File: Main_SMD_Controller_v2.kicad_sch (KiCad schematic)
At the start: 76 parts, among them J101 ETB43034G000Z, J102 ETB43034G000Z, J103 B2B-XH-A, J104 PH-1X3SG, J105 PCB-20, J106 B2B-XH-A, J107 PCB-20, J108 PH-1X2SG, J109 PCB-20, J110 PCB-20, P101 Eoshi-chan_Silk, P102 Serial_QR, U101 XC6201P332MR-G, U102 XC6902N331MR-G, U103 TC4066BP, U104 ADA4510-2ARZ, U105 MCP1501-20E/CHY, U106 LT1167CN8, U107 NJU7098A

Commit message: 念のため
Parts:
- J103: value B2B-XH-A -> B2P3-VH-3.3(LF)(SN); footprint Connector_JST:JST_XH_B2B-XH-A_1x02_P2.50mm_Vertical -> Connector_JST:JST_VH_B2P3-VH_1x02_P7.92mm_Vertical
- R107, R110, R111: footprint Resistor_THT:R_Axial_DIN0207_L6.3mm_D2.5mm_P2.54mm_Vertical -> Resistor_THT:R_Axial_DIN0207_L6.3mm_D2.5mm_P10.16mm_Horizontal
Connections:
- net GAIN2: now also U103.12; no longer U103.6
- net GAIN3: now also U103.6; no longer U103.12
- net ADC_Vref: now reaches R112.1, TP103.1, U105.1 (OUT)
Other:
- sheet Interface ports: added ADC_Vref; removed none
- note added: "Memo: GAIN2,3を入れ替える GreenPAKのFWを変更"
- moved on the sheet: TP103
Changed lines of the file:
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@@
 		)
 	)
+	(text "Memo: GAIN2,3を入れ替える GreenPAKのFWを変更"
+		(exclude_from_sim no)
+		(at 142.24 116.84 0)
+		(effects
+			(font
+				(size 1.27 1.27)
+			)
+		)
+	)
 	(text "V_{IN}=1/40*V_{SENS}"
 		(exclude_from_sim no)
@@
 	(text "2.048V"
 		(exclude_from_sim no)
-		(at 208.28 130.81 0)
+		(at 208.28 134.62 0)
 		(effects
 			(font
@@
 	)
 	(junction
-		(at 213.36 132.08)
-		(diameter 0)
-		(color 0 0 0 0)
-	)
-	(junction
 		(at 67.31 162.56)
 		(diameter 0)
@@
 	)
 	(junction
+		(at 204.47 132.08)
+		(diameter 0)
+		(color 0 0 0 0)
+	)
+	(junction
 		(at 181.61 124.46)
 		(diameter 0)
@@
 	(wire
 		(pts
-			(xy 213.36 128.27) (xy 213.36 132.08)
+			(xy 204.47 128.27) (xy 204.47 132.08)
 		)
 		(stroke
@@
 	(wire
 		(pts
+			(xy 204.47 132.08) (xy 213.36 132.08)
+		)
+		(stroke
+			(width 0)
+			(type default)
+		)
+	)
+	(wire
+		(pts
 			(xy 116.84 26.67) (xy 121.92 26.67)
 		)
@@
 	(wire
 		(pts
-			(xy 203.2 132.08) (xy 213.36 132.08)
+			(xy 203.2 132.08) (xy 204.47 132.08)
+		)
+		(stroke
+			(width 0)
+			(type default)
+		)
+	)
+	(wire
+		(pts
+			(xy 57.15 63.5) (xy 59.69 63.5)
 		)
 		(stroke
@@
 		)
 	)
+	(label "GAIN2"
+		(at 121.92 113.03 0)
+		(effects
+			(font
+				(size 1.27 1.27)
+			)
+			(justify left bottom)
+		)
+	)
 	(label "Vmeas"
 		(at 59.69 58.42 0)
@@
 		)
 	)
+	(label "ADC_Vref"
+		(at 213.36 132.08 0)
+		(effects
+			(font
+				(size 1.27 1.27)
+			)
+			(justify left bottom)
+		)
+	)
+	(label "ADC_Vref"
+		(at 59.69 63.5 0)
+		(effects
+			(font
+				(size 1.27 1.27)
+			)
+			(justify left bottom)
+		)
+	)
 	(label "rt"
 		(at 220.98 63.5 180)
@@
 		)
 	)
+	(label "GAIN3"
+		(at 121.92 101.6 0)
+		(effects
+			(font
+				(size 1.27 1.27)
+			)
+			(justify left bottom)
+		)
+	)
 	(label "RLY_LOUT"
 		(at 59.69 48.26 0)
@@
 		)
 	)
-	(label "GAIN2"
-		(at 121.92 101.6 0)
-		(effects
-			(font
-				(size 1.27 1.27)
-			)
-			(justify left bottom)
-		)
-	)
 	(label "Imeas"
 		(at 201.93 87.63 180)
@@
 		)
 	)
-	(label "GAIN3"
-		(at 121.92 113.03 0)
-		(effects
-			(font
-				(size 1.27 1.27)
-			)
-			(justify left bottom)
-		)
-	)
 	(label "RLY_LOUT"
 		(at 238.76 33.02 180)
@@
 			)
 		)
-		(property "Value" "B2B-XH-A"
+		(property "Value" "B2P3-VH-3.3(LF)(SN)"
 			(at 212.09 29.2099 0)
 			(show_name no)
@@
 			)
 		)
-		(property "Footprint" "Connector_JST:JST_XH_B2B-XH-A_1x02_P2.50mm_Vertical"
+		(property "Footprint" "Connector_JST:JST_VH_B2P3-VH_1x02_P7.92mm_Vertical"
 			(at 209.55 26.67 0)
 			(hide yes)
@@
 	(symbol
 		(lib_id "Connector:TestPoint_Probe")
-		(at 213.36 128.27 0)
+		(at 204.47 128.27 0)
 		(unit 1)
 		(body_style 1)
@@
 		(dnp no)
 		(property "Reference" "TP103"
-			(at 217.17 125.73 0)
+			(at 208.28 125.73 0)
 			(show_name no)
 			(do_not_autoplace no)
@@
 		)
 		(property "Value" "RCTCTE"
-			(at 217.17 128.27 0)
+			(at 208.28 128.27 0)
 			(show_name no)
 			(do_not_autoplace no)
@@
 		)
 		(property "Footprint" "AM_Conn_TP:RCTCE"
-			(at 218.44 128.27 0)
+			(at 209.55 128.27 0)
 			(hide yes)
 			(show_name no)
@@
 		)
 		(property "Datasheet" ""
-			(at 218.44 128.27 0)
+			(at 209.55 128.27 0)
 			(hide yes)
 			(show_name no)
@@
 		)
 		(property "Description" "test point (alternative probe-style design)"
-			(at 213.36 128.27 0)
+			(at 204.47 128.27 0)
 			(hide yes)
 			(show_name no)
@@
 		)
 		(property "Description_1" ""
-			(at 213.36 128.27 0)
+			(at 204.47 128.27 0)
 			(hide yes)
 			(show_name no)
@@
 		)
 		(property "Sengoku_code" ""
-			(at 213.36 128.27 0)
+			(at 204.47 128.27 0)
 			(hide yes)
 			(show_name no)
@@
 			)
 		)
-		(property "Footprint" "Resistor_THT:R_Axial_DIN0207_L6.3mm_D2.5mm_P2.54mm_Vertical"
+		(property "Footprint" "Resistor_THT:R_Axial_DIN0207_L6.3mm_D2.5mm_P10.16mm_Horizontal"
 			(at 163.83 28.448 90)
 			(hide yes)
@@
 			)
 		)
-		(property "Footprint" "Resistor_THT:R_Axial_DIN0207_L6.3mm_D2.5mm_P2.54mm_Vertical"
+		(property "Footprint" "Resistor_THT:R_Axial_DIN0207_L6.3mm_D2.5mm_P10.16mm_Horizontal"
 			(at 204.978 48.26 90)
 			(hide yes)
@@
 			)
 		)
-		(property "Footprint" "Resistor_THT:R_Axial_DIN0207_L6.3mm_D2.5mm_P2.54mm_Vertical"
+		(property "Footprint" "Resistor_THT:R_Axial_DIN0207_L6.3mm_D2.5mm_P10.16mm_Horizontal"
 			(at 204.978 58.42 90)
 			(hide yes)
@@
 		(members "403ef226-6633-4c83-ab8a-01415e3ffac7" "ab16d228-7bd2-4212-bd9b-7f549ffd1b8f")
 	)
-	(group ""
-		(members "403ef226-6633-4c83-ab8a-01415e3ffac7" "ab16d228-7bd2-4212-bd9b-7f549ffd1b8f")
-	)
 	(sheet
 		(at 223.52 58.42)
@@
 	(sheet
 		(at 40.64 34.29)
-		(size 16.51 30.48)
+		(size 16.51 31.75)
 		(exclude_from_sim no)
 		(in_bom yes)
@@
 		)
 		(property "Sheetfile" "v2_interface.kicad_sch"
-			(at 40.64 65.786 0)
+			(at 40.64 67.31 0)
 			(show_name no)
 			(do_not_autoplace no)
@@
 			(effects
 				(font
+					(size 1.27 1.27)
+				)
+				(justify right)
+			)
+		)
+		(pin "ADC_Vref" input
+			(at 57.15 63.5 0)
+			(effects
+				(font

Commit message: 部品配置
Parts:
- added R117: 0, Resistor_SMD:R_0805_2012Metric, symbol Device:R
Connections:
- net GND: now also R117.2
- net GNDA: now also R117.1
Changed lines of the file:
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@@
 	)
 	(junction
+		(at 191.77 62.23)
+		(diameter 0)
+		(color 0 0 0 0)
+	)
+	(junction
 		(at 147.32 39.37)
 		(diameter 0)
@@
 	(wire
 		(pts
+			(xy 181.61 62.23) (xy 180.34 62.23)
+		)
+		(stroke
+			(width 0)
+			(type default)
+		)
+	)
+	(wire
+		(pts
 			(xy 52.07 128.27) (xy 52.07 130.81)
 		)
@@
 	(wire
 		(pts
-			(xy 213.36 156.21) (xy 213.36 158.75)
+			(xy 189.23 62.23) (xy 191.77 62.23)
 		)
 		(stroke
@@
 	(wire
 		(pts
-			(xy 228.6 102.87) (xy 228.6 105.41)
+			(xy 213.36 156.21) (xy 213.36 158.75)
 		)
 		(stroke
@@
 	(wire
 		(pts
+			(xy 191.77 62.23) (xy 191.77 63.5)
+		)
+		(stroke
+			(width 0)
+			(type default)
+		)
+	)
+	(wire
+		(pts
 			(xy 158.75 73.66) (xy 160.02 73.66)
 		)
@@
 	(wire
 		(pts
+			(xy 237.49 102.87) (xy 238.76 102.87)
+		)
+		(stroke
+			(width 0)
+			(type default)
+		)
+	)
+	(wire
+		(pts
 			(xy 104.14 170.18) (xy 104.14 172.72)
 		)
@@
 	(wire
 		(pts
+			(xy 203.2 63.5) (xy 203.2 62.23)
+		)
+		(stroke
+			(width 0)
+			(type default)
+		)
+	)
+	(wire
+		(pts
 			(xy 57.15 41.91) (xy 67.31 41.91)
 		)
@@
 	(wire
 		(pts
-			(xy 229.87 102.87) (xy 228.6 102.87)
-		)
-		(stroke
-			(width 0)
-			(type default)
-		)
-	)
-	(wire
-		(pts
 			(xy 148.59 85.09) (xy 151.13 85.09)
 		)
@@
 	(wire
 		(pts
-			(xy 238.76 92.71) (xy 238.76 102.87)
+			(xy 180.34 62.23) (xy 180.34 63.5)
 		)
 		(stroke
@@
 	(wire
 		(pts
+			(xy 228.6 102.87) (xy 229.87 102.87)
+		)
+		(stroke
+			(width 0)
+			(type default)
+		)
+	)
+	(wire
+		(pts
 			(xy 212.09 85.09) (xy 213.36 85.09)
 		)
@@
 		)
 	)
+	(wire
+		(pts
+			(xy 228.6 102.87) (xy 228.6 105.41)
+		)
+		(stroke
+			(width 0)
+			(type default)
+		)
+	)
 	(bus
 		(pts
@@
 	(wire
 		(pts
-			(xy 237.49 102.87) (xy 238.76 102.87)
-		)
-		(stroke
-			(width 0)
-			(type default)
-		)
-	)
-	(wire
-		(pts
 			(xy 113.03 73.66) (xy 113.03 85.09)
 		)
@@
 		)
 	)
+	(wire
+		(pts
+			(xy 238.76 92.71) (xy 238.76 102.87)
+		)
+		(stroke
+			(width 0)
+			(type default)
+		)
+	)
 	(table
 		(column_count 2)
@@
 	)
 	(symbol
+		(lib_name "GND_1")
+		(lib_id "power:GND")
+		(at 180.34 63.5 0)
+		(unit 1)
+		(body_style 1)
+		(exclude_from_sim no)
+		(in_bom yes)
+		(on_board yes)
+		(in_pos_files yes)
+		(dnp no)
+		(fields_autoplaced yes)
+		(property "Reference" "#PWR0145"
+			(at 180.34 69.85 0)
+			(hide yes)
+			(show_name no)
+			(do_not_autoplace no)
+			(effects
+				(font
+					(size 1.27 1.27)
+				)
+			)
+		)
+		(property "Value" "GND"
+			(at 180.34 68.58 0)
+			(show_name no)
+			(do_not_autoplace no)
+			(effects
+				(font
+					(size 1.27 1.27)
+				)
+			)
+		)
+		(property "Footprint" ""
+			(at 180.34 63.5 0)
+			(hide yes)
+			(show_name no)
+			(do_not_autoplace no)
+			(effects
+				(font
+					(size 1.27 1.27)
+				)
+			)
+		)
+		(property "Datasheet" ""
+			(at 180.34 63.5 0)
+			(hide yes)
+			(show_name no)
+			(do_not_autoplace no)
+			(effects
+				(font
+					(size 1.27 1.27)
+				)
+			)
+		)
+		(property "Description" "Power symbol creates a global label with name \"GND\" , ground"
+			(at 180.34 63.5 0)
+			(hide yes)
+			(show_name no)
+			(do_not_autoplace no)
+			(effects
+				(font
+					(size 1.27 1.27)
+				)
+			)
+		)
+		(pin "1"
+		)
+		(instances
+			(project "Main_SMD_Controller_v2"
+				(path "/ad678d38-2bf7-47ec-94cd-212edb6f07b2"
+					(reference "#PWR0145")
+					(unit 1)
+				)
+			)
+		)
+	)
+	(symbol
 		(lib_id "power:-3V3")
 		(at 170.18 55.88 180)
@@
 	(symbol
 		(lib_id "power:GNDA")
-		(at 203.2 62.23 0)
+		(at 203.2 63.5 0)
 		(unit 1)
 		(body_style 1)
@@
 		(fields_autoplaced yes)
 		(property "Reference" "#PWR0126"
-			(at 203.2 68.58 0)
+			(at 203.2 69.85 0)
 			(hide yes)
 			(show_name no)
@@
 		)
 		(property "Value" "GNDA"
-			(at 203.2 67.31 0)
+			(at 203.2 68.58 0)
 			(show_name no)
 			(do_not_autoplace no)
@@
 		)
 		(property "Footprint" ""
-			(at 203.2 62.23 0)
+			(at 203.2 63.5 0)
 			(hide yes)
 			(show_name no)
@@
 		)
 		(property "Datasheet" ""
-			(at 203.2 62.23 0)
+			(at 203.2 63.5 0)
 			(hide yes)
 			(show_name no)
@@
 		)
 		(property "Description" "Power symbol creates a global label with name \"GNDA\" , analog ground"
-			(at 203.2 62.23 0)
+			(at 203.2 63.5 0)
 			(hide yes)
 			(show_name no)
@@
 	(symbol
 		(lib_id "power:GNDA")
-		(at 191.77 62.23 0)
+		(at 191.77 63.5 0)
 		(unit 1)
 		(body_style 1)
@@
 		(fields_autoplaced yes)
 		(property "Reference" "#PWR0122"
-			(at 191.77 68.58 0)
+			(at 191.77 69.85 0)
 			(hide yes)
 			(show_name no)
@@
 		)
 		(property "Value" "GNDA"
-			(at 191.77 67.31 0)
+			(at 191.77 68.58 0)
 			(show_name no)
 			(do_not_autoplace no)
@@
 		)
 		(property "Footprint" ""
-			(at 191.77 62.23 0)
+			(at 191.77 63.5 0)
 			(hide yes)
 			(show_name no)
@@
 		)
 		(property "Datasheet" ""
-			(at 191.77 62.23 0)
+			(at 191.77 63.5 0)
 			(hide yes)
 			(show_name no)
@@
 		)
 		(property "Description" "Power symbol creates a global label with name \"GNDA\" , analog ground"
-			(at 191.77 62.23 0)
+			(at 191.77 63.5 0)
 			(hide yes)
 			(show_name no)
@@
 					(unit 1)
 				)
+			)
+		)
+	)
+	(symbol
+		(lib_id "Device:R")
+		(at 185.42 62.23 270)
+		(unit 1)
+		(body_style 1)
+		(exclude_from_sim no)
+		(in_bom yes)
+		(on_board yes)
+		(in_pos_files yes)
+		(dnp no)
+		(property "Reference" "R117"
+			(at 185.42 66.04 90)
+			(show_name no)
+			(do_not_autoplace no)
+			(effects
+				(font
+					(size 1.27 1.27)
+				)
+			)
+		)
+		(property "Value" "0"
+			(at 185.42 68.58 90)
+			(show_name no)
+			(do_not_autoplace no)
+			(effects
+				(font
+					(size 1.27 1.27)
+				)
+			)
+		)
+		(property "Footprint" "Resistor_SMD:R_0805_2012Metric"
+			(at 185.42 60.452 90)
+			(hide yes)
+			(show_name no)
+			(do_not_autoplace no)
+			(effects
+				(font
+					(size 1.27 1.27)
+				)
+			)
+		)
+		(property "Datasheet" ""
+			(at 185.42 62.23 0)
+			(hide yes)
+			(show_name no)
+			(do_not_autoplace no)
+			(effects
+				(font
+					(size 1.27 1.27)
+				)
+			)
+		)
+		(property "Description" "Resistor"
+			(at 185.42 62.23 0)
+			(hide yes)
+			(show_name no)
+			(do_not_autoplace no)
+			(effects
+				(font
+					(size 1.27 1.27)
+				)
+			)
+		)
+		(pin "2"
+		)
+		(pin "1"
+		)
+		(instances
+			(project "Main_SMD_Controller_v2"
+				(path "/ad678d38-2bf7-47ec-94cd-212edb6f07b2"
+					(reference "R117")
+					(unit 1)
+				)

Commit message: ほぼ完成?
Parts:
- added C124, C125: 47u, Capacitor_SMD:CP_Elec_6.3x5.9, symbol Device:C_Polarized_Small
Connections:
- net GND: now also C124.2, C125.1
- net VCC: now also C124.1
- net VEE: now also C125.2

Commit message: ほぼ完成
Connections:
- net GNDA: now also U104.3; no longer U104.5
- net Vin: now also U104.5; no longer U104.3
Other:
- moved on the sheet: C118

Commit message: アノテーション変更前
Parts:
- added J111: B2B-XH-A, Connector_JST:JST_XH_B2B-XH-A_1x02_P2.50mm_Vertical, symbol Connector_Generic:Conn_01x02
- added J112: PH-1X3SG, Connector_PinHeader_2.54mm:PinHeader_1x03_P2.54mm_Vertical, symbol Connector_Generic:Conn_01x03
- FB101, FB102: footprint Inductor_SMD:L_0805_2012Metric -> Inductor_THT:L_Axial_L5.3mm_D2.2mm_P2.54mm_Vertical_Vishay_IM-1
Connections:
- net GND: now also J111.2 (Pin_2)
- net rt: now also J112.2 (Pin_2)
- new net: J111.1 (Pin_1), J112.3 (Pin_3)
- new net Interface/rt: J112.1 (Pin_1)

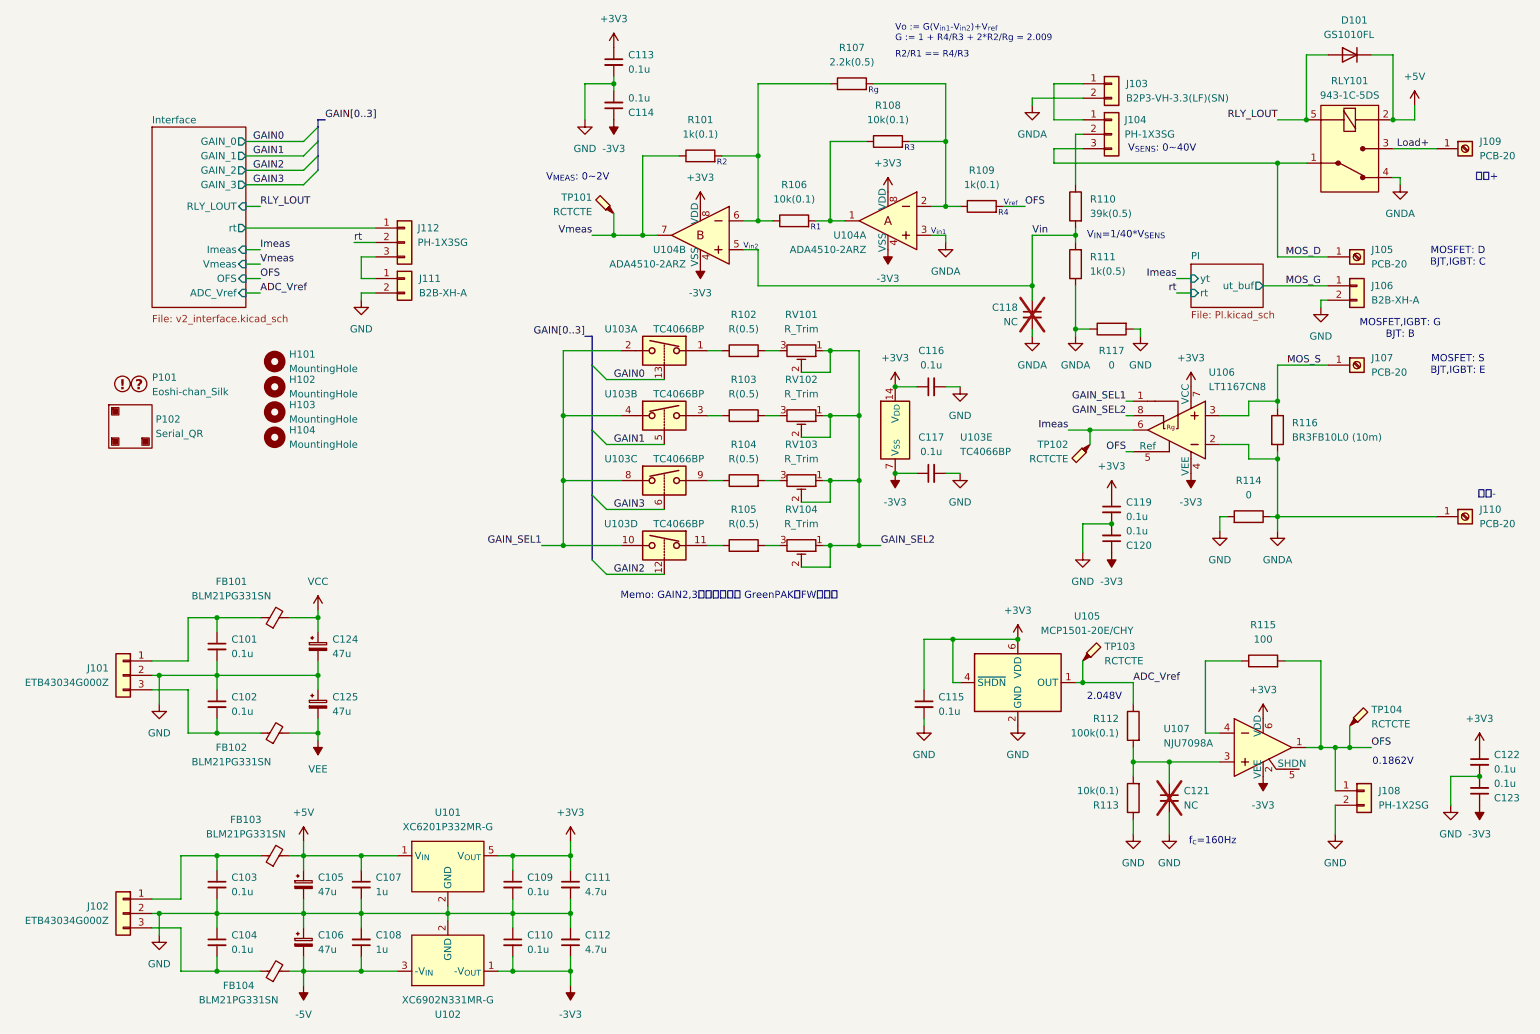
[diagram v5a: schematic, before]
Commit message: アノテーションリセット 余計なもんも消す
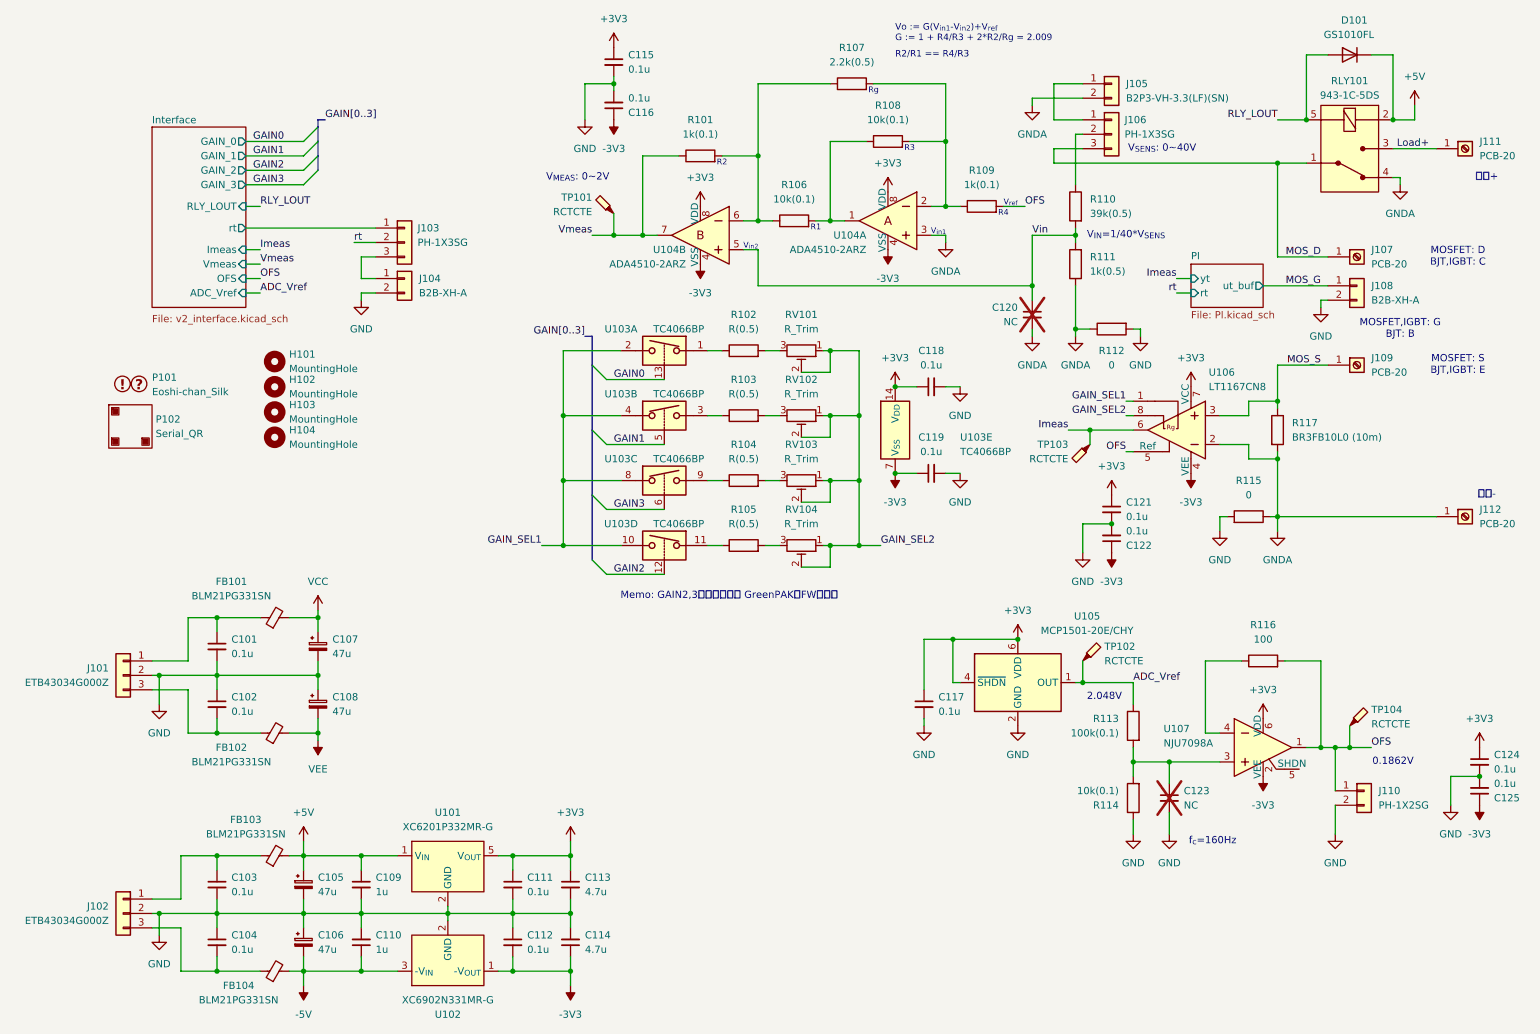
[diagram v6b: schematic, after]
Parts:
- renumbered C124 to C107, C125 to C108, C107 to C109, C108 to C110, C109 to C111, C110 to C112, C111 to C113, C112 to C114, C113 to C115, C114 to C116, C115 to C117, C116 to C118, C117 to C119, C118 to C120, C119 to C121, C120 to C122, C121 to C123, C122 to C124, C123 to C125, J112 to J103, J111 to J104, J103 to J105, J104 to J106, J105 to J107, J106 to J108, J107 to J109, J108 to J110, J109 to J111, J110 to J112, R117 to R112, R112 to R113, R113 to R114, R114 to R115, R115 to R116, R116 to R117, TP103 to TP102, TP102 to TP103

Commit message: 完成
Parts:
- removed P102: Serial_QR, JLCPCB_Serial:Serial_QR_5x5, symbol JLCPCB_Serial:Serial_QR
- P101: footprint Eoshi-chan_v2:Eoshi-chan-v2_10x10 -> Eoshi-chan_v2:Eoshi-chan-v2_7x7
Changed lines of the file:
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@@
 			)
 		)
-		(property "Footprint" "Eoshi-chan_v2:Eoshi-chan-v2_10x10"
+		(property "Footprint" "Eoshi-chan_v2:Eoshi-chan-v2_7x7"
 			(at 37.338 76.962 0)
 			(hide yes)
@@
 					(unit 1)
 				)
-			)
-		)
-	)
-	(symbol
-		(lib_id "JLCPCB_Serial:Serial_QR")
-		(at 36.83 86.995 0)
-		(unit 1)
-		(body_style 1)
-		(exclude_from_sim yes)
-		(in_bom no)
-		(on_board yes)
-		(in_pos_files yes)
-		(dnp no)
-		(fields_autoplaced yes)
-		(property "Reference" "P102"
-			(at 41.275 85.7249 0)
-			(show_name no)
-			(do_not_autoplace no)
-			(effects
-				(font
-					(size 1.27 1.27)
-				)
-				(justify left)
-			)
-		)
-		(property "Value" "Serial_QR"
-			(at 41.275 88.2649 0)
-			(show_name no)
-			(do_not_autoplace no)
-			(effects
-				(font
-					(size 1.27 1.27)
-				)
-				(justify left)
-			)
-		)
-		(property "Footprint" "JLCPCB_Serial:Serial_QR_5x5"
-			(at 36.83 86.995 0)
-			(hide yes)
-			(show_name no)
-			(do_not_autoplace no)
-			(effects
-				(font
-					(size 1.27 1.27)
-				)
-			)
-		)
-		(property "Datasheet" ""
-			(at 36.83 86.995 0)
-			(hide yes)
-			(show_name no)
-			(do_not_autoplace no)
-			(effects
-				(font
-					(size 1.27 1.27)
-				)
-			)
-		)
-		(property "Description" ""
-			(at 36.83 86.995 0)
-			(show_name no)
-			(do_not_autoplace no)
-			(effects
-				(font
-					(size 1.27 1.27)
-				)
-			)
-		)
-		(property "Akizuki_code" ""
-			(at 36.83 86.995 0)
-			(hide yes)
-			(show_name no)
-			(do_not_autoplace no)
-			(effects
-				(font
-					(size 1.27 1.27)
-				)
-			)
-		)
-		(property "Marutsu_code" ""
-			(at 36.83 86.995 0)
-			(hide yes)
-			(show_name no)
-			(do_not_autoplace no)
-			(effects
-				(font
-					(size 1.27 1.27)
-				)
-			)
-		)
-		(property "URL" ""
-			(at 36.83 86.995 0)
-			(show_name no)
-			(do_not_autoplace no)
-			(effects
-				(font
-					(size 1.27 1.27)
-				)
-			)
-		)
-		(property "Description_1" ""
-			(at 36.83 86.995 0)
-			(hide yes)
-			(show_name no)
-			(do_not_autoplace no)
-			(effects
-				(font
-					(size 1.27 1.27)
-				)
-			)
-		)
-		(property "Sengoku_code" ""
-			(at 36.83 86.995 0)
-			(hide yes)
-			(show_name no)
-			(do_not_autoplace no)
-			(effects
-				(font
-					(size 1.27 1.27)
-				)
-			)
-		)
-		(instances
-			(project "Main_SMD_Controller_v2"
-				(path "/ad678d38-2bf7-47ec-94cd-212edb6f07b2"
-					(reference "P102")
-					(unit 1)
-				)
